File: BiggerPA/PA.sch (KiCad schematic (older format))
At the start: 123 parts, among them J1 Conn_Coaxial, J10 Conn_01x01, J12 Conn_01x01, J13 Conn_01x01, J14 Conn_01x01, J16 Conn_01x01, J2 Conn_01x02, J27 Conn_01x01, J3 Conn_Coaxial, J4 Conn_01x02, J5 Conn_01x02, J6 Conn_01x01, J7 Conn_01x01, J8 Conn_01x01, J9 Conn_01x01, Q1 2N3906, Q10 IRF510N, Q11 IRF510N, Q14 IRF510N, Q15 IRF510N, Q2 IRF510N, Q3 IRF510N, Q5 2N3906, Q6 IRF510N, Q7 IRF510N, T1 Transformer_1P1Sdotted, T2 Transformer_1P1Sdotted, T3 Transformer_1P1Sdotted, U1 LM7805_TO220

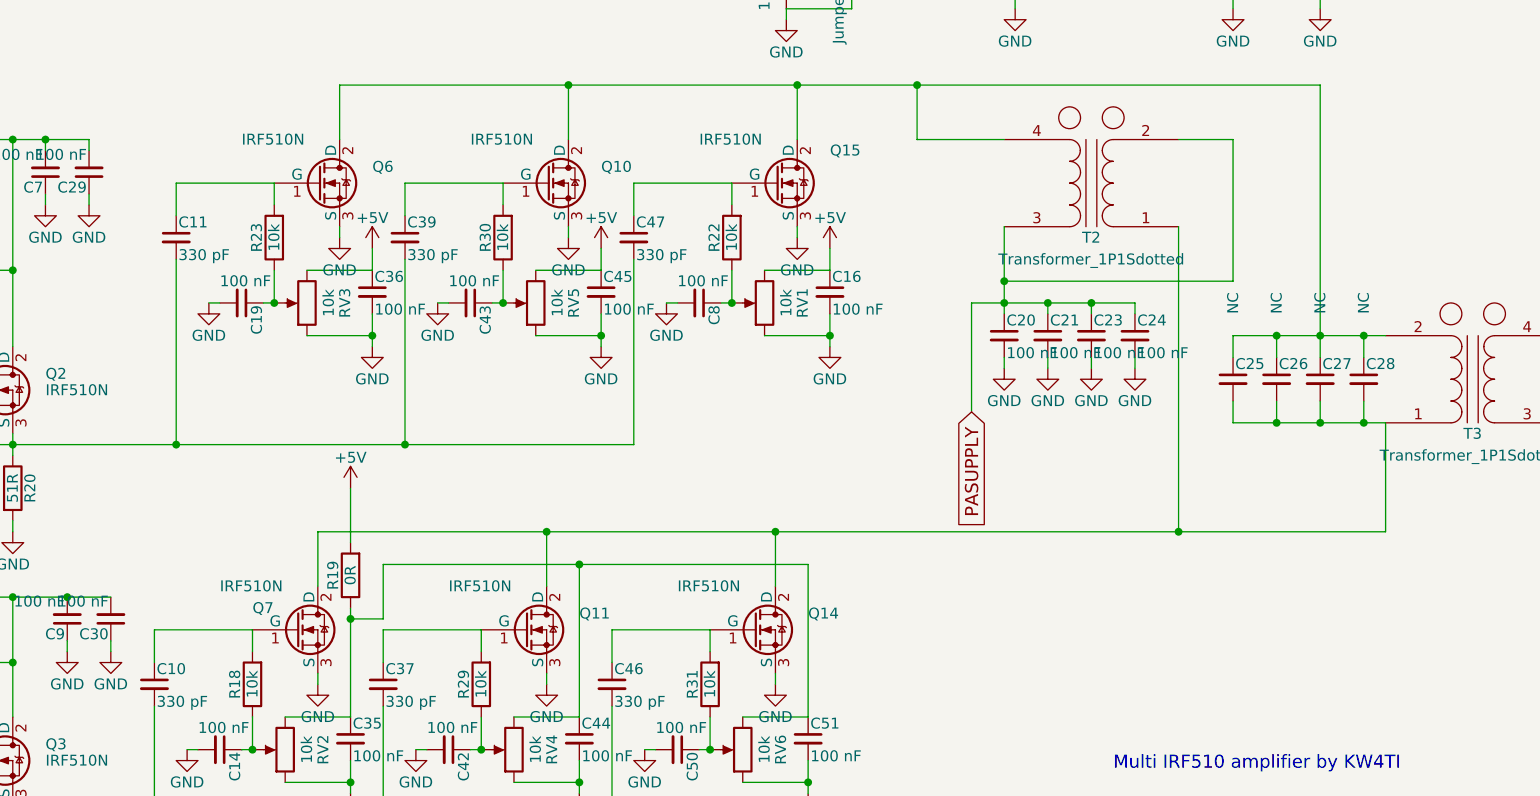
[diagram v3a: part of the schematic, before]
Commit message: Added gate resistors to BiggerPA
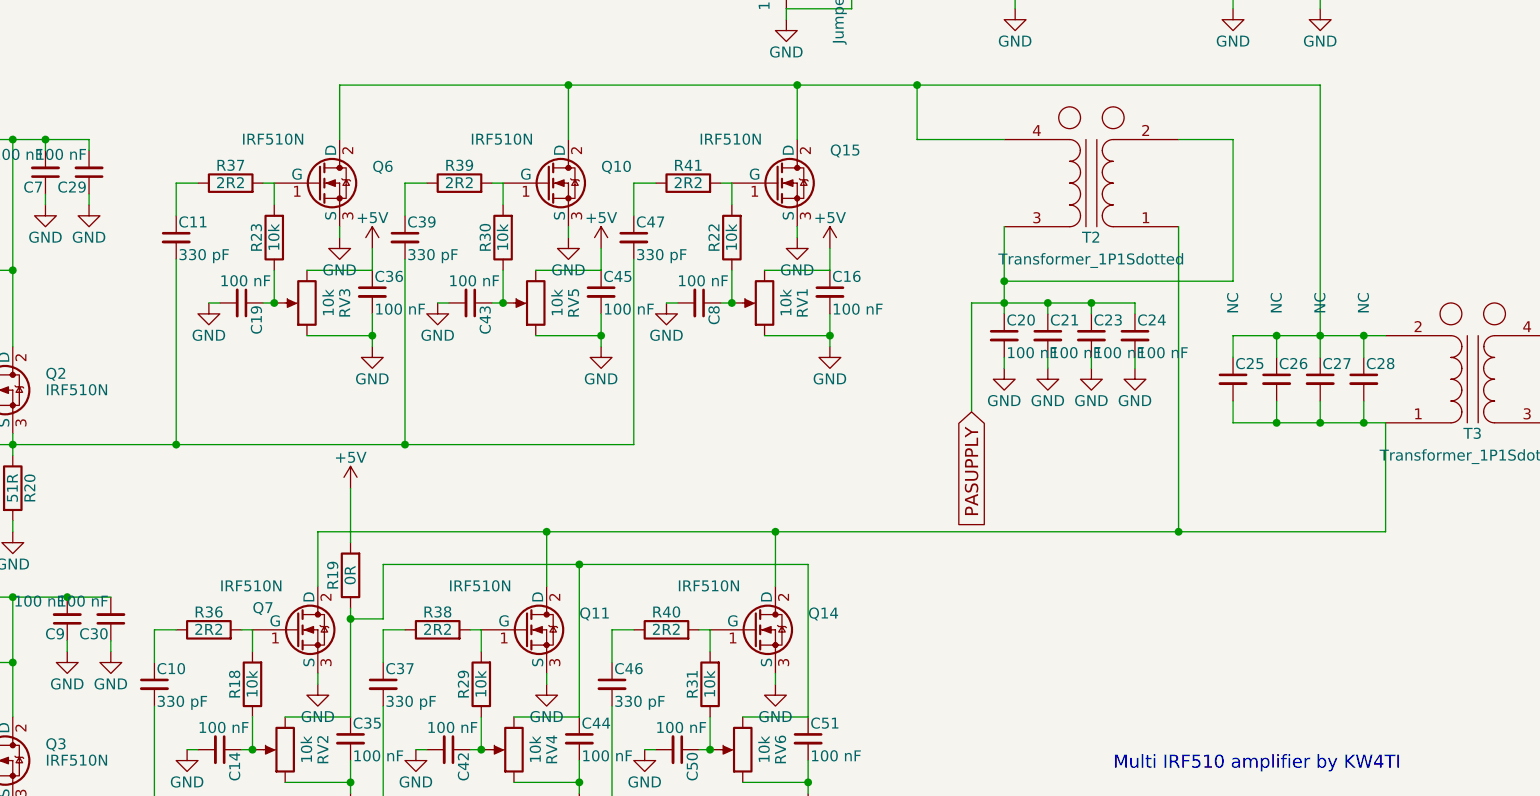
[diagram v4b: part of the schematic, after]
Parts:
- added R36, R37, R38, R39, R40, R41: 2R2, Resistors_THT:R_Axial_DIN0207_L6.3mm_D2.5mm_P10.16mm_Horizontal, symbol R
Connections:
- net at Q15.1 (G), R22.2: now also R41.2; no longer C47.1
- net at Q10.1 (G), R30.2: now also R39.2; no longer C39.1
- net at Q6.1 (G), R23.2: now also R37.2; no longer C11.1
- net at Q14.1 (G), R31.2: now also R40.2; no longer C46.1
- net at Q11.1 (G), R29.2: now also R38.2; no longer C37.1
- net at Q7.1 (G), R18.2: now also R36.2; no longer C10.1
- new net: C47.1, R41.1
- new net: C39.1, R39.1
- new net: C11.1, R37.1
- new net: C46.1, R40.1
- new net: C37.1, R38.1
- new net: C10.1, R36.1
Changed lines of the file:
@@
 	9250 5200 9250 5700
 Wire Wire Line
-	4350 5700 9250 5700
+	9250 5700 4350 5700
 Connection ~ 8300 5700
 Wire Wire Line
@@
 Wire Wire Line
 	5800 4250 5800 4100
-Wire Wire Line
-	5800 4100 6250 4100
 Connection ~ 6250 4650
 Wire Wire Line
@@
 Wire Wire Line
 	4750 4250 4750 4100
-Wire Wire Line
-	4750 4100 5200 4100
 Connection ~ 5200 4650
 Wire Wire Line
@@
 Wire Wire Line
 	3700 4250 3700 4100
-Wire Wire Line
-	3700 4100 4150 4100
 Connection ~ 4150 4650
 Wire Wire Line
@@
 Wire Wire Line
 	5700 6300 5700 6150
-Wire Wire Line
-	5700 6150 6150 6150
 Connection ~ 6150 6700
 Wire Wire Line
@@
 Wire Wire Line
 	4650 6300 4650 6150
-Wire Wire Line
-	4650 6150 5100 6150
 Connection ~ 5100 6700
 Wire Wire Line
@@
 Wire Wire Line
 	3600 6300 3600 6150
-Wire Wire Line
-	3600 6150 4050 6150
 Connection ~ 4050 6700
 Wire Wire Line
@@
 Wire Wire Line
 	7550 3150 7550 3300
+Wire Wire Line
+	4050 6150 4000 6150
+Wire Wire Line
+	3600 6150 3700 6150
+$Comp
+L R R38
+U 1 1 5D3270C8
+P 4900 6150
+F 0 "R38" V 4980 6150 50  0000 C CNN
+F 1 "2R2" V 4900 6150 50  0000 C CNN
+F 2 "Resistors_THT:R_Axial_DIN0207_L6.3mm_D2.5mm_P10.16mm_Horizontal" V 4830 6150 50  0001 C CNN
+F 3 "" H 4900 6150 50  0001 C CNN
+	1    4900 6150
+	0    -1   -1   0
+$EndComp
+Wire Wire Line
+	5100 6150 5050 6150
+Wire Wire Line
+	4650 6150 4750 6150
+$Comp
+L R R40
+U 1 1 5D32771A
+P 5950 6150
+F 0 "R40" V 6030 6150 50  0000 C CNN
+F 1 "2R2" V 5950 6150 50  0000 C CNN
+F 2 "Resistors_THT:R_Axial_DIN0207_L6.3mm_D2.5mm_P10.16mm_Horizontal" V 5880 6150 50  0001 C CNN
+F 3 "" H 5950 6150 50  0001 C CNN
+	1    5950 6150
+	0    -1   -1   0
+$EndComp
+Wire Wire Line
+	6150 6150 6100 6150
+Wire Wire Line
+	5700 6150 5800 6150
+$Comp
+L R R37
+U 1 1 5D32813C
+P 3950 4100
+F 0 "R37" V 4030 4100 50  0000 C CNN
+F 1 "2R2" V 3950 4100 50  0000 C CNN
+F 2 "Resistors_THT:R_Axial_DIN0207_L6.3mm_D2.5mm_P10.16mm_Horizontal" V 3880 4100 50  0001 C CNN
+F 3 "" H 3950 4100 50  0001 C CNN
+	1    3950 4100
+	0    -1   -1   0
+$EndComp
+Wire Wire Line
+	4150 4100 4100 4100
+Wire Wire Line
+	3700 4100 3800 4100
+$Comp
+L R R39
+U 1 1 5D3287A5
+P 5000 4100
+F 0 "R39" V 5080 4100 50  0000 C CNN
+F 1 "2R2" V 5000 4100 50  0000 C CNN
+F 2 "Resistors_THT:R_Axial_DIN0207_L6.3mm_D2.5mm_P10.16mm_Horizontal" V 4930 4100 50  0001 C CNN
+F 3 "" H 5000 4100 50  0001 C CNN
+	1    5000 4100
+	0    -1   -1   0
+$EndComp
+Wire Wire Line
+	5200 4100 5150 4100
+Wire Wire Line
+	4750 4100 4850 4100
+$Comp
+L R R41
+U 1 1 5D328D9C
+P 6050 4100
+F 0 "R41" V 6130 4100 50  0000 C CNN
+F 1 "2R2" V 6050 4100 50  0000 C CNN
+F 2 "Resistors_THT:R_Axial_DIN0207_L6.3mm_D2.5mm_P10.16mm_Horizontal" V 5980 4100 50  0001 C CNN
+F 3 "" H 6050 4100 50  0001 C CNN
+	1    6050 4100
+	0    -1   -1   0
+$EndComp
+Wire Wire Line
+	6250 4100 6200 4100
+Wire Wire Line
+	5800 4100 5900 4100
+$Comp
+L R R36
+U 1 1 5D327C79
+P 3850 6150
+F 0 "R36" V 3930 6150 50  0000 C CNN
+F 1 "2R2" V 3850 6150 50  0000 C CNN
+F 2 "Resistors_THT:R_Axial_DIN0207_L6.3mm_D2.5mm_P10.16mm_Horizontal" V 3780 6150 50  0001 C CNN
+F 3 "" H 3850 6150 50  0001 C CNN
+	1    3850 6150
+	0    -1   -1   0
+$EndComp
 $EndSCHEMATC

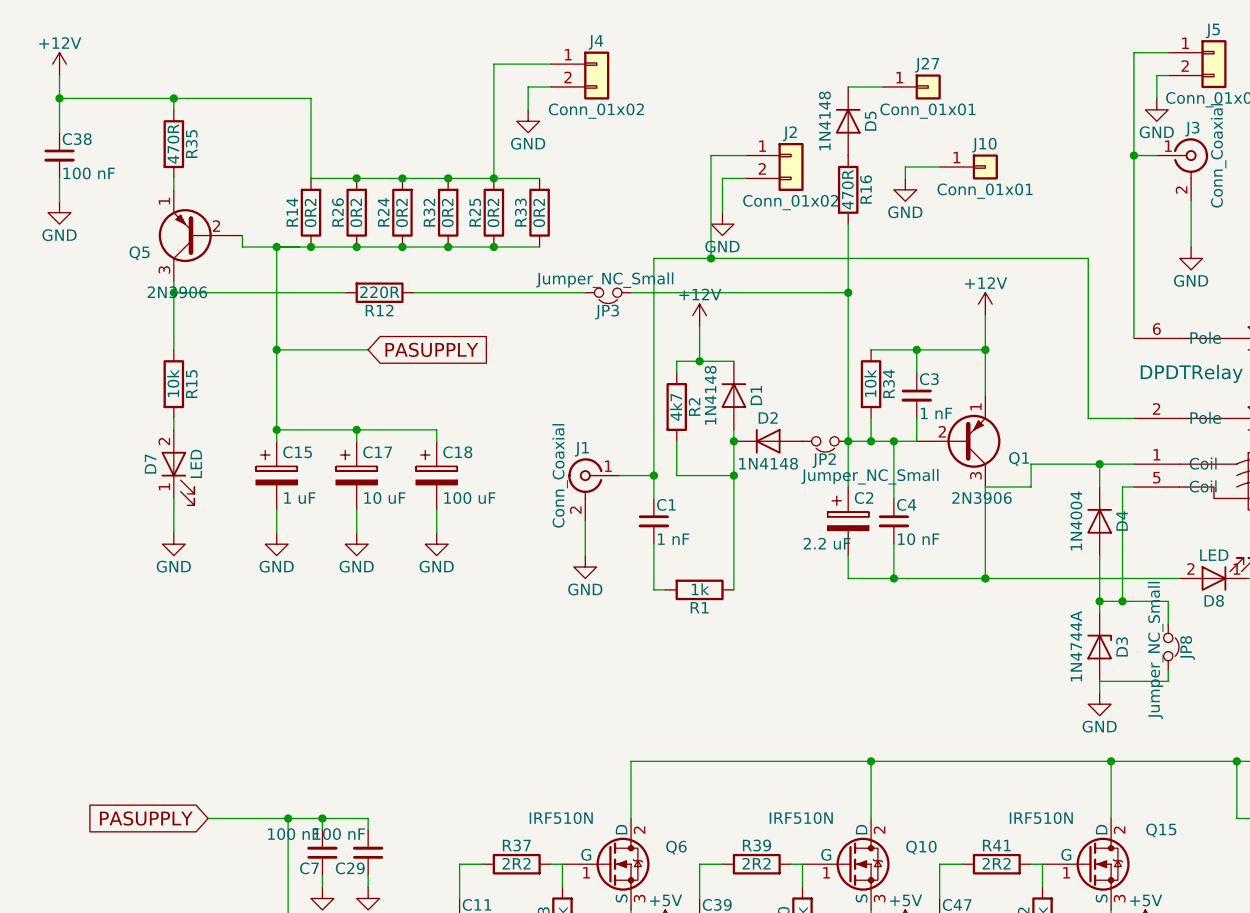
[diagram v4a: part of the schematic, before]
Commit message: Changed rig RX/TX control
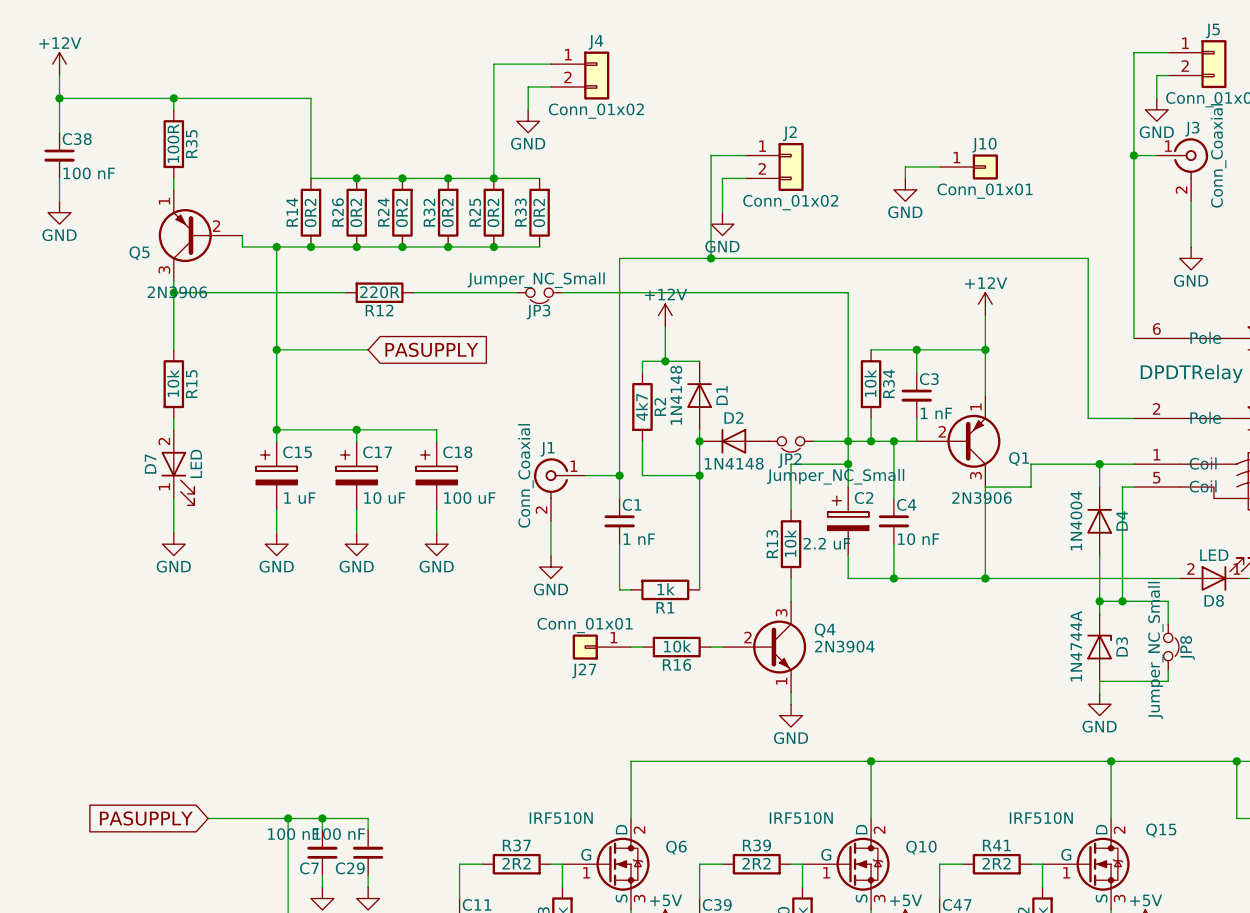
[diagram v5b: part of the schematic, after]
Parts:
- removed D5: 1N4148, Diodes_THT:D_DO-35_SOD27_P7.62mm_Horizontal, symbol D
- added Q4: 2N3904, TO_SOT_Packages_THT:TO-92_Molded_Narrow, symbol 2N3904
- added R13: 10k, Resistors_THT:R_Axial_DIN0207_L6.3mm_D2.5mm_P7.62mm_Horizontal, symbol R
- R16: value 470R -> 10k
- R35: value 470R -> 100R
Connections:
- net GND: now also Q4.1 (E)
- net at C2.1, C3.2, C4.1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: now also R13.2; no longer R16.2
- net at R16.1: now also Q4.2 (B)
- net at J27.1 (Pin_1): now also R16.2
- new net: Q4.3 (C), R13.1
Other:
- moved on the sheet: C1, D1, D2, J1, J27, JP2, JP3, R1, R16, R2

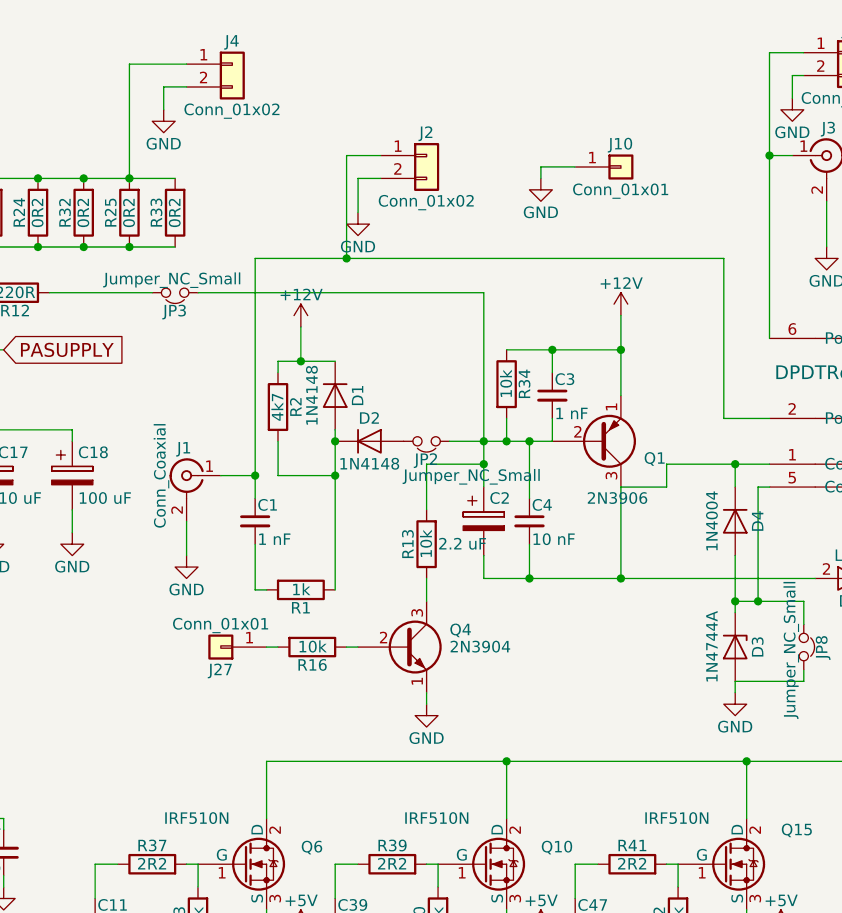
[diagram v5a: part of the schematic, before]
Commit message: Fixed polarity of rig RXTX relay grounding
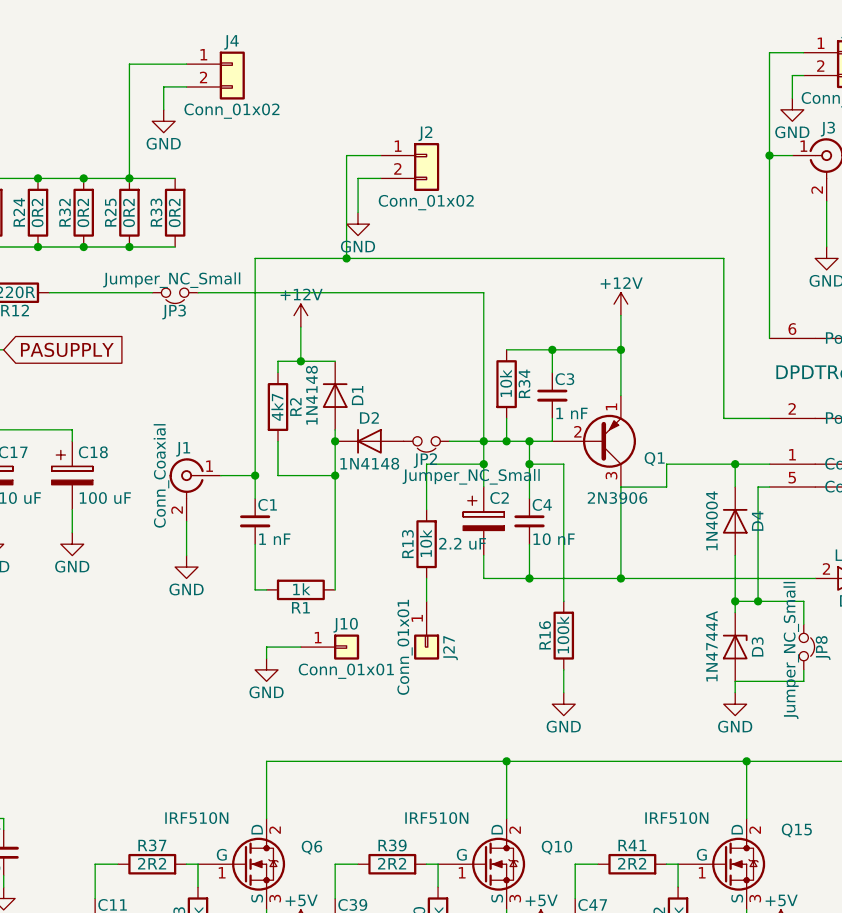
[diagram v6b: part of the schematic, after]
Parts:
- removed Q4: 2N3904, TO_SOT_Packages_THT:TO-92_Molded_Narrow, symbol 2N3904
- R16: value 10k -> 100k
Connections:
- net GND: now also R16.1
- net at C2.1, C3.2, C4.1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: now also R16.2
- net at J27.1 (Pin_1): now also R13.1; no longer R16.2
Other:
- moved on the sheet: J10, J27
